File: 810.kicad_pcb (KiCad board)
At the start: 2 copper layers, 148 x 110 mm, 334 parts, among them J1 PJ301BM, J10 PJ301BM, J11 PJ301BM, J12 PJ301BM, J13 PJ301BM, J14 PJ301BM, J15 JACK_MONO_SW, J16 PJ301BM, J17 PJ301B, J18 PJ301B, J2 PJ301BM, J3 PJ301BM, J4 PJ301B, J5 PJ301B, J6 PJ301BM, J7 PJ301BM, J8 PJ301BM, J9 PJ301BM, P1 CONN_01X08, P2 CONN_02X05, P3 CONN_01X03, P4 CONN_01X08, P5 CONN_01X02, P6 CONN_02X03, Q1 PMBT2369, Q10 2SK208-GR, Q11 2SC4738, Q12 2SA1832, Q13 2SA1832, Q14 2SA1832, Q15 2SC4738, Q2 2SK208-GR, Q3 2SA1618, Q4 2SC4207, Q5 2SK208-GR, Q6 MMBF4391LT1G, Q7 2SA1832, Q8 PMBT2369, Q9 2SK208-GR, SW1 SPDT, SW2 SPDT, SW3 BF3-1050, SW4 SPDT, SW5 DP6T-ALPHA-SR2511, U1 TL072-, U10 TL072-, U11 TL072-, U12 TA75S558F, U13 TA75S558F, U14 TA75S558F, U15 TA75S558F, U16 TA75S558F, U17 CD4052, U18 TA75S558F, U19 TL072-, U2 TL072-, U20 CD4013, U21 TA75S558F, U3 TL072-, U4 CD40106, U5 CD4027, U6 LM13700, U7 LM13700, U8 LM13700, U9 TL072-

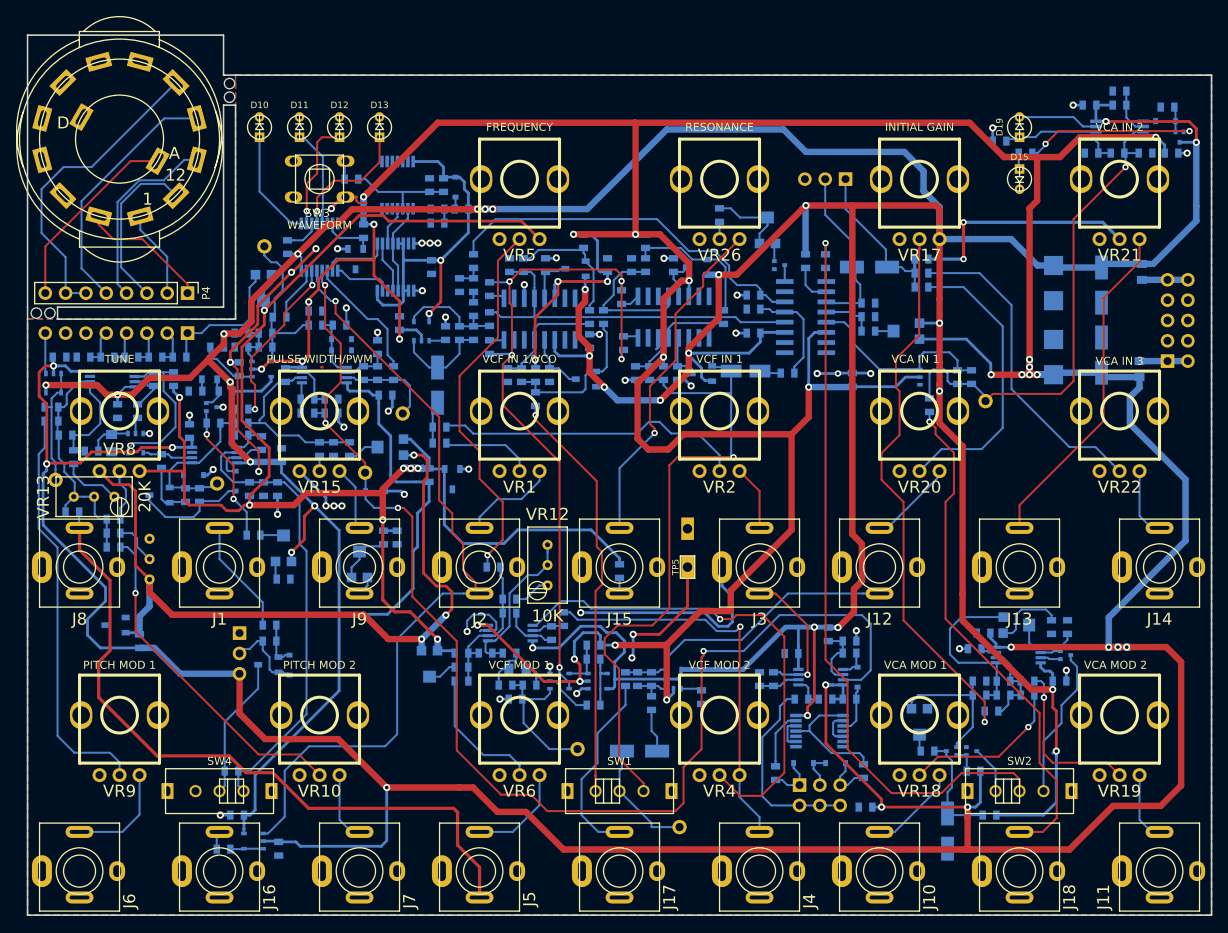
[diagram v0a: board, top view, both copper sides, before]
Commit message: 4 layer version amost done with dedicated ground plane and power plane
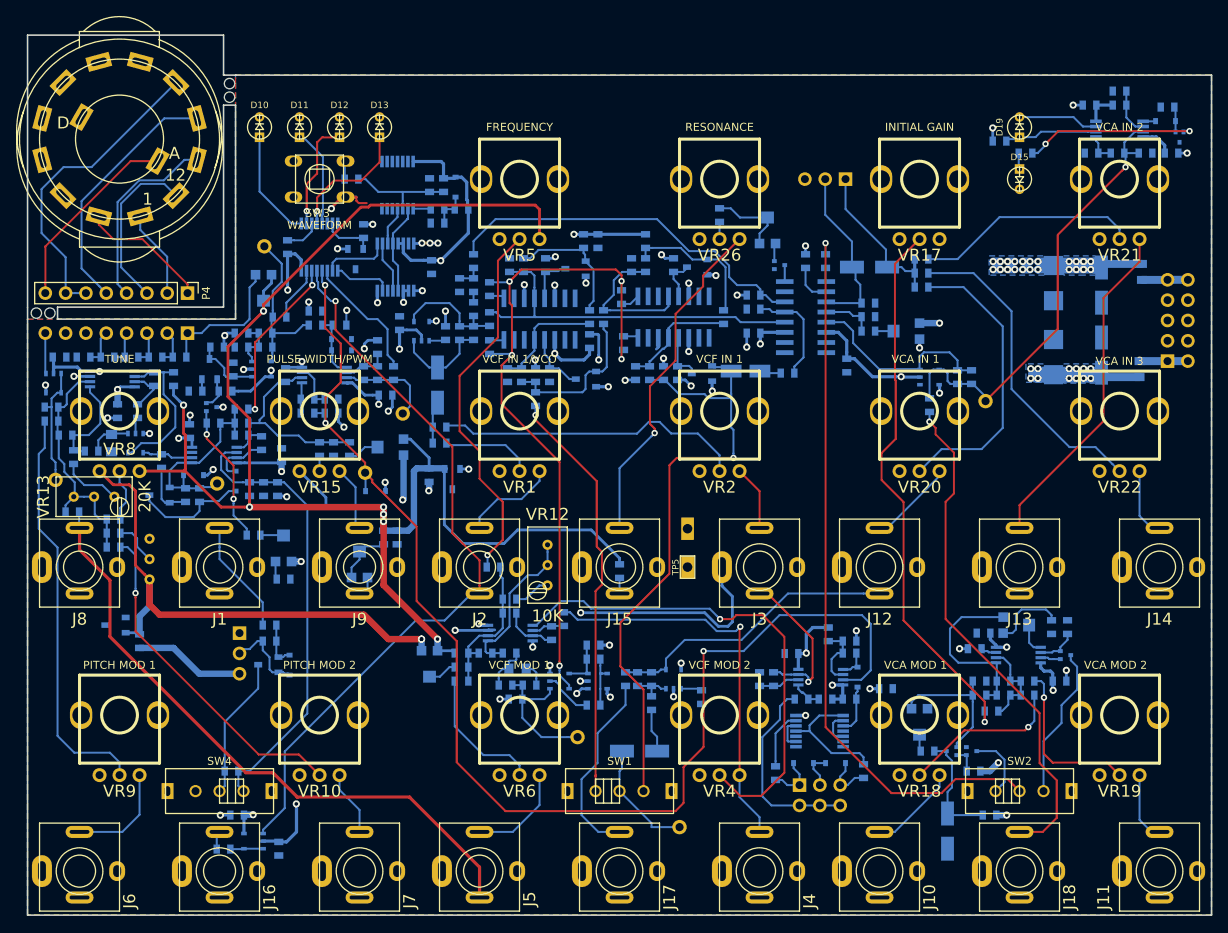
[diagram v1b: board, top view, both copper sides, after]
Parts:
- moved C48 15.0 mm to (191.3, 122.7), turned to 180 degrees
- moved C35 3.23 mm to (155.3, 66.8), turned to 90 degrees
- moved C32 1.93 mm to (186.4, 82.3), turned to 90 degrees
- moved TP1 1.50 mm to (152.8, 128.8)
- moved R68 0.75 mm to (109.7, 82.8)
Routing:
- net -12V: track 825.7 -> 671.8 mm, vias 37 -> 35
- net GND: track 158.1 -> 101.2 mm, vias 50 -> 40
- net +12V: track 734.5 -> 701.3 mm, vias 30 -> 53
- net KYBD: track 88.0 -> 79.1 mm
- net VCO: track 98.9 -> 93.0 mm
- net Net-(C22-Pad2): track 62.8 -> 57.8 mm
- net -10V: track 95.5 -> 91.0 mm
- net Net-(C21-Pad2): track 82.5 -> 78.7 mm
- net +10V: track 198.0 -> 201.4 mm, vias 8 -> 7
- net Net-(Q12-Pad3): track 6.00 -> 8.31 mm
- net SUB_OSC: track 18.2 -> 19.8 mm
- net Net-(R105-Pad2): track 92.4 -> 90.9 mm
- net Net-(R78-Pad1): track 29.4 -> 27.9 mm, vias 2 -> 0
- net VCO_PULSE: track 158.1 -> 159.2 mm, vias 4 -> 3
- net Net-(C3-Pad2): track 13.5 -> 14.4 mm
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- added copper zone on B.Cu, net +12V
- added copper zone on In1.Cu, net +12V
- added copper zone on In1.Cu, net -12V
- added copper zone on In2.Cu, net GND
- removed copper zone on B.Cu, net +10V
- removed copper zone on F.Cu, net +12V
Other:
- copper layers 2 -> 4

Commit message: little more ground plane tweaking required, tidy up silk screen then done
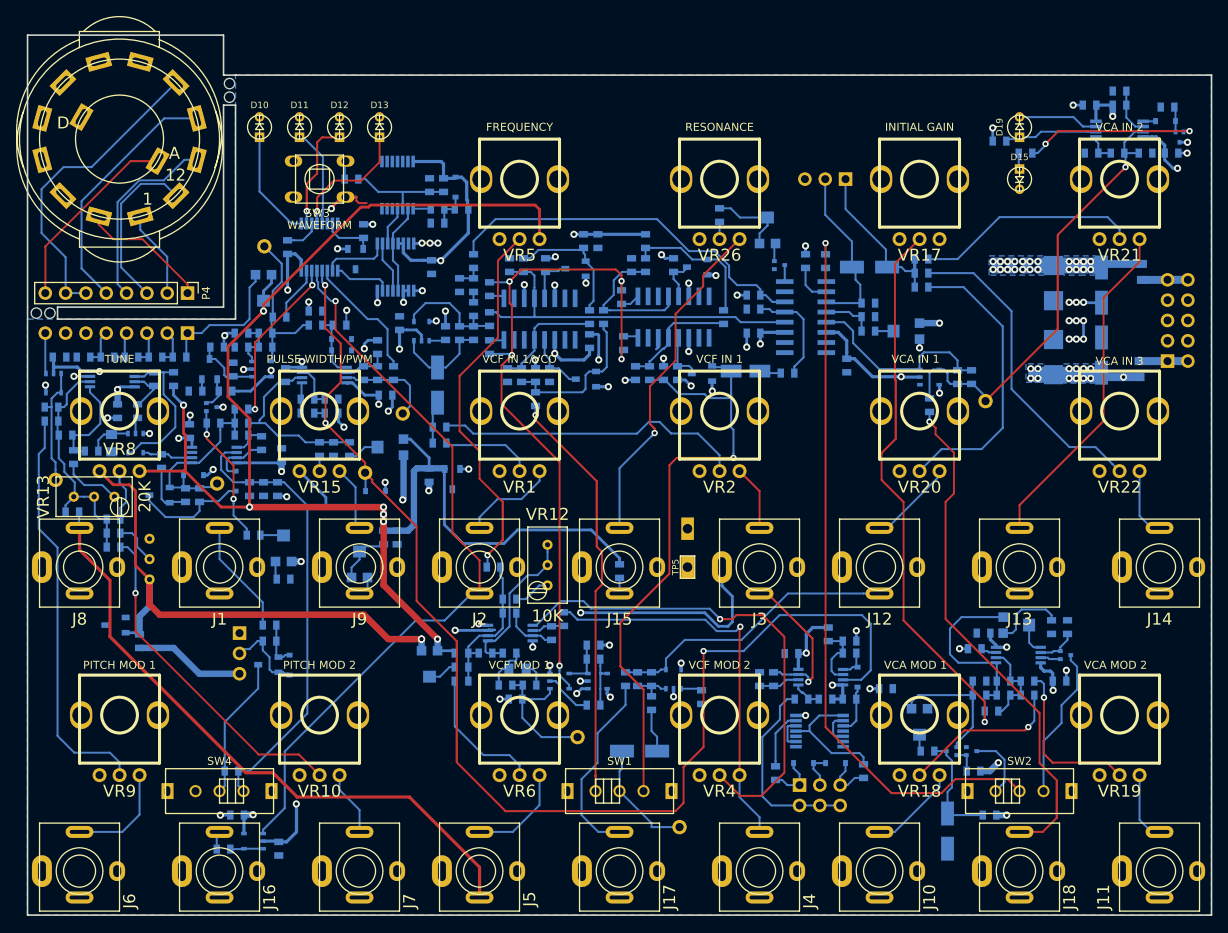
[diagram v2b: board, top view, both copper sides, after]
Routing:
- net +12V: track 701.3 -> 733.2 mm, vias 53 -> 55
- net -12V: track 671.8 -> 703.5 mm, vias 35 -> 37
- net GND: track 101.2 -> 115.8 mm, vias 40 -> 49
- removed copper zone on F.Cu, net GND
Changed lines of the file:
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@@
   (general
     (links 679)
-    (no_connects 4)
-    (area 78.467857 38.411038 232.878334 151.100001)
+    (no_connects 1)
+    (area 83.899999 40.899999 232.100001 151.100001)
     (thickness 1.6)
     (drawings 148)
-    (tracks 2234)
+    (tracks 2275)
     (zones 0)
     (modules 334)
@@
   (layers
     (0 F.Cu signal)
-    (1 In1.Cu power hide)
-    (2 In2.Cu power hide)
+    (1 In1.Cu power)
+    (2 In2.Cu power)
     (31 B.Cu signal)
     (32 B.Adhes user)
@@
   )
   (setup
-    (last_trace_width 0.8)
+    (last_trace_width 0.25)
     (user_trace_width 0.25)
     (user_trace_width 0.4)
@@
   (segment (start 148.635 73.90158) (end 148.635 70.7159) (width 0.25) (layer B.Cu) (net 9))
   (segment (start 148.635 70.7159) (end 148.75 70.6009) (width 0.25) (layer B.Cu) (net 9))
+  (segment (start 215.999998 79) (end 216 78.999998) (width 0.35) (layer In2.Cu) (net 10))
+  (segment (start 215.1 79) (end 215.999998 79) (width 0.35) (layer In2.Cu) (net 10))
+  (segment (start 216 76.7) (end 216 78.999998) (width 0.35) (layer B.Cu) (net 10))
+  (via (at 216 78.999998) (size 0.9) (drill 0.45) (layers F.Cu B.Cu) (net 10))
+  (segment (start 214.2 74.4) (end 214.2 76.7) (width 0.35) (layer In2.Cu) (net 10))
+  (segment (start 214.2 76.7) (end 214.2 79) (width 0.35) (layer In2.Cu) (net 10))
+  (segment (start 215.1 76.7) (end 214.2 76.7) (width 0.35) (layer B.Cu) (net 10))
+  (via (at 214.2 76.7) (size 0.9) (drill 0.45) (layers F.Cu B.Cu) (net 10))
+  (segment (start 216 76.7) (end 215.1 76.7) (width 0.35) (layer In2.Cu) (net 10))
+  (via (at 215.1 76.7) (size 0.9) (drill 0.45) (layers F.Cu B.Cu) (net 10))
+  (via (at 216 76.7) (size 0.9) (drill 0.45) (layers F.Cu B.Cu) (net 10))
+  (segment (start 214.2 79) (end 215.1 79) (width 0.35) (layer B.Cu) (net 10))
+  (via (at 215.1 79) (size 0.9) (drill 0.45) (layers F.Cu B.Cu) (net 10))
+  (via (at 214.2 79) (size 0.9) (drill 0.45) (layers F.Cu B.Cu) (net 10))
+  (segment (start 215.1 74.4) (end 214.2 74.4) (width 0.35) (layer B.Cu) (net 10))
+  (via (at 214.2 74.4) (size 0.9) (drill 0.45) (layers F.Cu B.Cu) (net 10))
+  (segment (start 216 74.4) (end 215.1 74.4) (width 0.35) (layer In2.Cu) (net 10))
+  (via (at 215.1 74.4) (size 0.9) (drill 0.45) (layers F.Cu B.Cu) (net 10))
+  (segment (start 218.25 74.44964) (end 216.04964 74.44964) (width 0.35) (layer B.Cu) (net 10))
+  (segment (start 216.04964 74.44964) (end 216 74.4) (width 0.35) (layer B.Cu) (net 10))
+  (via (at 216 74.4) (size 0.9) (drill 0.45) (layers F.Cu B.Cu) (net 10))
   (segment (start 128.7446 96.9446) (end 128.7 96.9) (width 0.35) (layer B.Cu) (net 10))
   (segment (start 128.7446 98) (end 128.7446 96.9446) (width 0.35) (layer B.Cu) (net 10))
@@
   (segment (start 197.3509 130.5) (end 198.85 130.5) (width 0.25) (layer B.Cu) (net 41))
   (segment (start 199.59874 138.8991) (end 199 138.30036) (width 0.25) (layer B.Cu) (net 41))
+  (segment (start 219.65 60.2) (end 219.65 54.6) (width 0.8) (layer In1.Cu) (net 42))
+  (segment (start 219.85 54.4) (end 219.65 54.6) (width 0.35) (layer In1.Cu) (net 42))
+  (segment (start 219.65 54.6) (end 219.65 51.15) (width 0.8) (layer In1.Cu) (net 42))
+  (segment (start 229 54.4) (end 219.85 54.4) (width 0.35) (layer In1.Cu) (net 42))
+  (segment (start 228 54.4) (end 229 54.4) (width 0.35) (layer B.Cu) (net 42))
+  (via (at 229 54.4) (size 0.9) (drill 0.45) (layers F.Cu B.Cu) (net 42))
+  (segment (start 215.1 69.3) (end 215.1 64.75) (width 0.8) (layer In1.Cu) (net 42))
+  (segment (start 215.1 64.75) (end 219.65 60.2) (width 0.8) (layer In1.Cu) (net 42))
+  (segment (start 219.6491 49.75) (end 219.6491 51.1491) (width 0.8) (layer B.Cu) (net 42))
+  (segment (start 219.6491 51.1491) (end 219.65 51.15) (width 0.8) (layer B.Cu) (net 42))
+  (via (at 219.65 51.15) (size 0.9) (drill 0.45) (layers F.Cu B.Cu) (net 42))
   (segment (start 169.57 85.470002) (end 169.599998 85.5) (width 0.4) (layer B.Cu) (net 42))
   (segment (start 169.57 84.2525) (end 169.57 85.470002) (width 0.4) (layer B.Cu) (net 42))
@@
   (segment (start 212.1 121.7991) (end 212.1491 121.75) (width 0.25) (layer B.Cu) (net 42))
   (segment (start 212.5 70.05036) (end 212.25 69.80036) (width 0.8) (layer B.Cu) (net 42))
-  (segment (start 223 83.75) (end 218.80036 83.75) (width 1) (layer B.Cu) (net 43))
+  (segment (start 223 83.75) (end 221 83.75) (width 1) (layer B.Cu) (net 43))
+  (segment (start 221 83.75) (end 218.80036 83.75) (width 1) (layer B.Cu) (net 43))
+  (segment (start 227.75 65.5) (end 221 72.25) (width 0.8) (layer In1.Cu) (net 43))
+  (segment (start 221 72.25) (end 221 83.75) (width 0.8) (layer In1.Cu) (net 43))
+  (via (at 221 83.75) (size 0.9) (drill 0.45) (layers F.Cu B.Cu) (net 43))
+  (segment (start 227.75 57.65) (end 227.75 65.5) (width 0.8) (layer In1.Cu) (net 43))
+  (segment (start 226.1491 55.75) (end 226.1491 56.5991) (width 0.35) (layer B.Cu) (net 43))
+  (segment (start 226.1491 56.5991) (end 227.2 57.65) (width 0.35) (layer B.Cu) (net 43))
+  (segment (start 227.2 57.65) (end 227.75 57.65) (width 0.35) (layer B.Cu) (net 43))
+  (via (at 227.75 57.65) (size 0.9) (drill 0.45) (layers F.Cu B.Cu) (net 43))
   (segment (start 218.80036 83.75) (end 218.25 83.19964) (width 1) (layer B.Cu) (net 43))
   (segment (start 205.35 131.95) (end 205.35 130.4) (width 0.8) (layer In1.Cu) (net 43))
@@
       )
     )
-  )
-  (zone (net 10) (net_name GND) (layer F.Cu) (hatch edge 0.508)
-    (connect_pads (clearance 0.254))
-    (min_thickness 0.2032)
-    (fill yes (arc_segments 16) (thermal_gap 0.254) (thermal_bridge_width 0.5048))
-    (polygon
-      (pts
-        (xy 110 46) (xy 232 46) (xy 232 151) (xy 84 151) (xy 84 76.5)
-        (xy 110 76.5) (xy 110 47)
-      )
-    )

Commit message: moved rotary switch to its own PCB
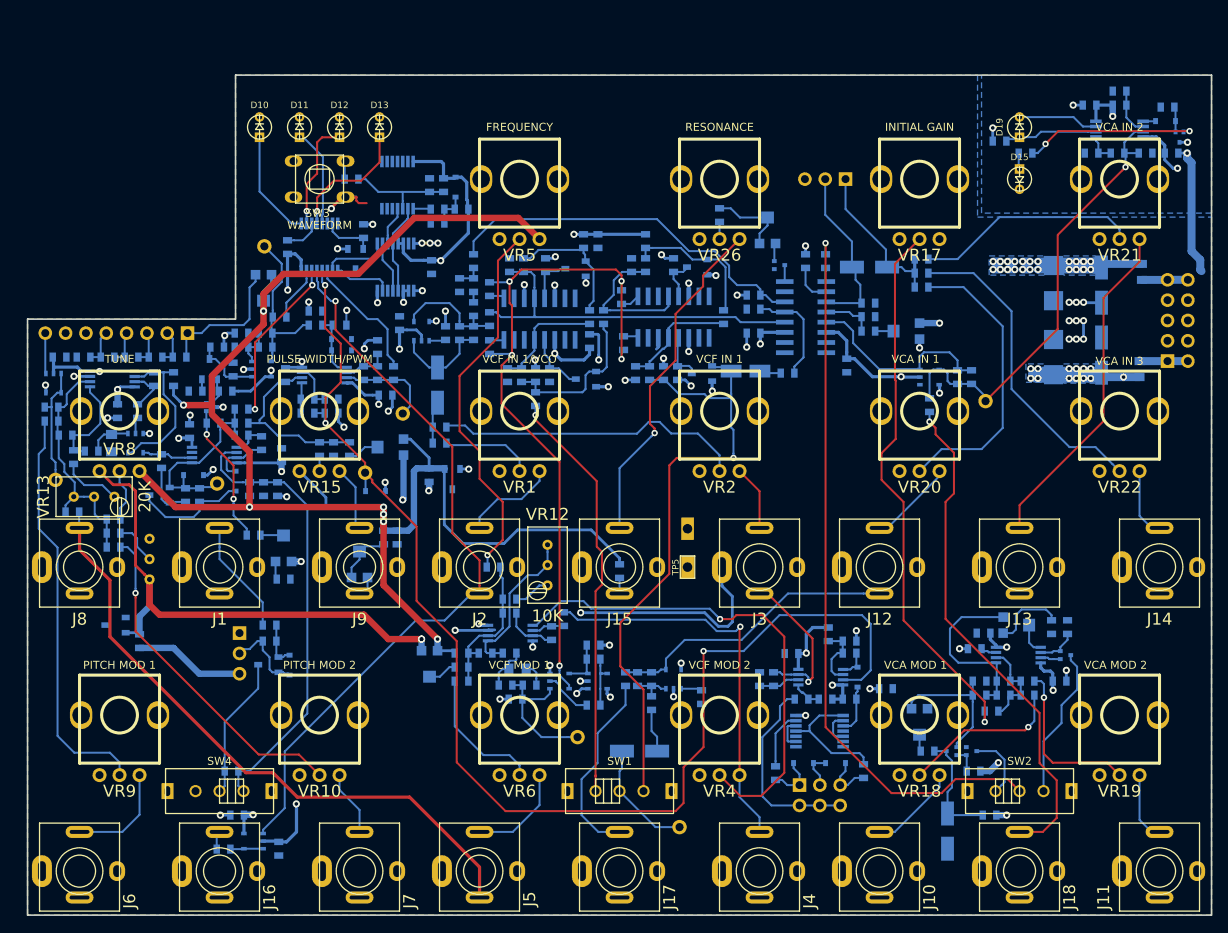
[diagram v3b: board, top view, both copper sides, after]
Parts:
- removed P4: CONN_01X08, Pin_Headers:Pin_Header_Straight_1x08_Pitch2.54mm
- removed SW5: DP6T-ALPHA-SR2511, MyModules:SR2511-ALPHA
- removed the TP7 at (109.2, 47.1)
- removed the TP7 at (109.2, 48.8)
- removed the TP7 at (85.1, 75.8)
- removed the TP7 at (86.8, 75.8)
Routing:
- net Net-(P4-Pad6): track 39.1 -> 0.00 mm
- net Net-(P4-Pad5): track 31.5 -> 0.00 mm
- net Net-(P4-Pad8): track 24.3 -> 0.00 mm
- net Net-(P4-Pad4): track 23.9 -> 0.00 mm
- net Net-(P4-Pad3): track 21.0 -> 0.00 mm
- net Net-(P4-Pad1): track 16.3 -> 0.00 mm
- net GND: track 115.8 -> 131.3 mm
- net Net-(P4-Pad2): track 11.0 -> 0.00 mm
- net +10V: track 201.4 -> 195.5 mm
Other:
- board size 148 x 110 mm -> 148 x 105 mm

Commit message: bit of tweaking. ready to order
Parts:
- TC1: footprint MyModules:SM0805-HAND -> MyModules:SM0603-R-JRL
- moved R128 4.78 mm to (220.2, 59.0), turned to 0 degrees
- moved TC1 0.22 mm to (94.7, 91.9)
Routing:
- net GND: track 131.3 -> 123.7 mm, vias 49 -> 54
- net Net-(C21-Pad2): track 78.7 -> 76.3 mm
- net KYBD: track 79.1 -> 81.1 mm
- net Net-(J18-Pad3): track 64.0 -> 63.3 mm
- net Net-(R78-Pad1): track 27.9 -> 27.3 mm

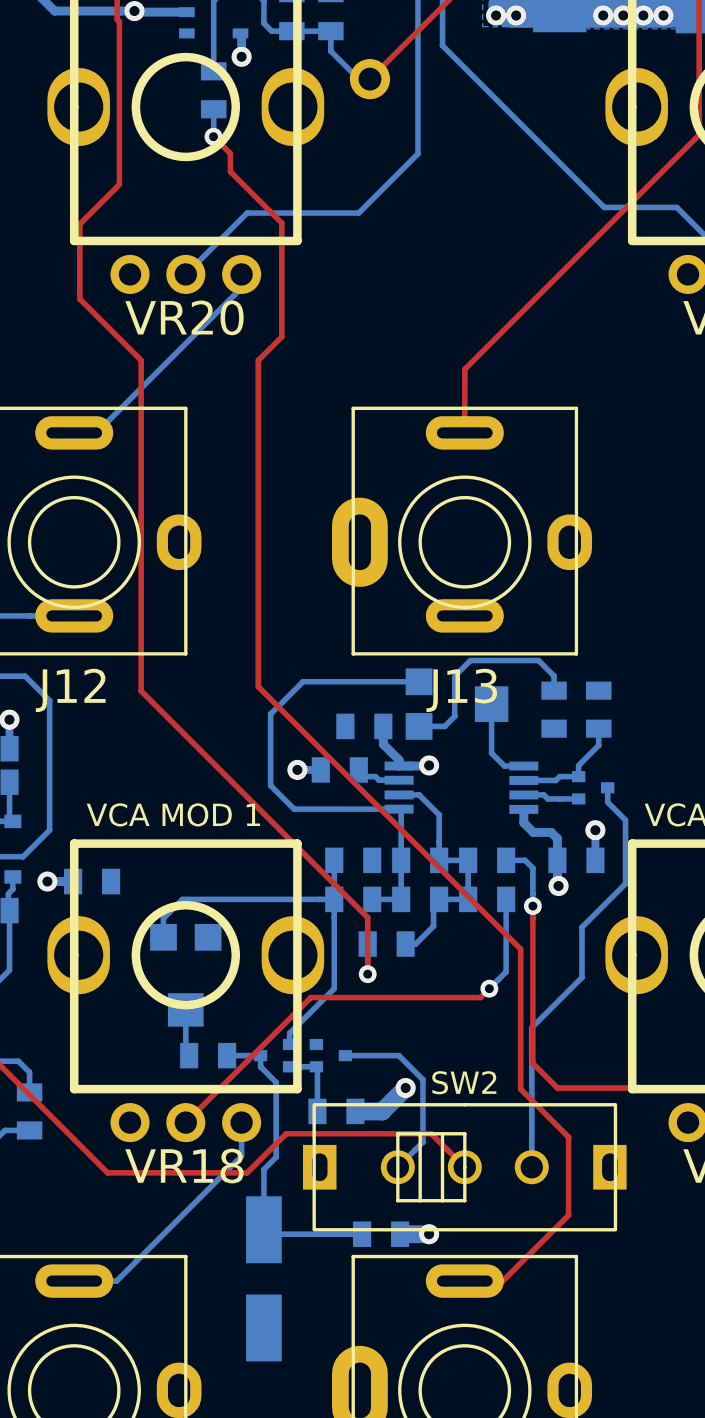
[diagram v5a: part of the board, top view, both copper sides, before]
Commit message: changed a couple of schematic notes
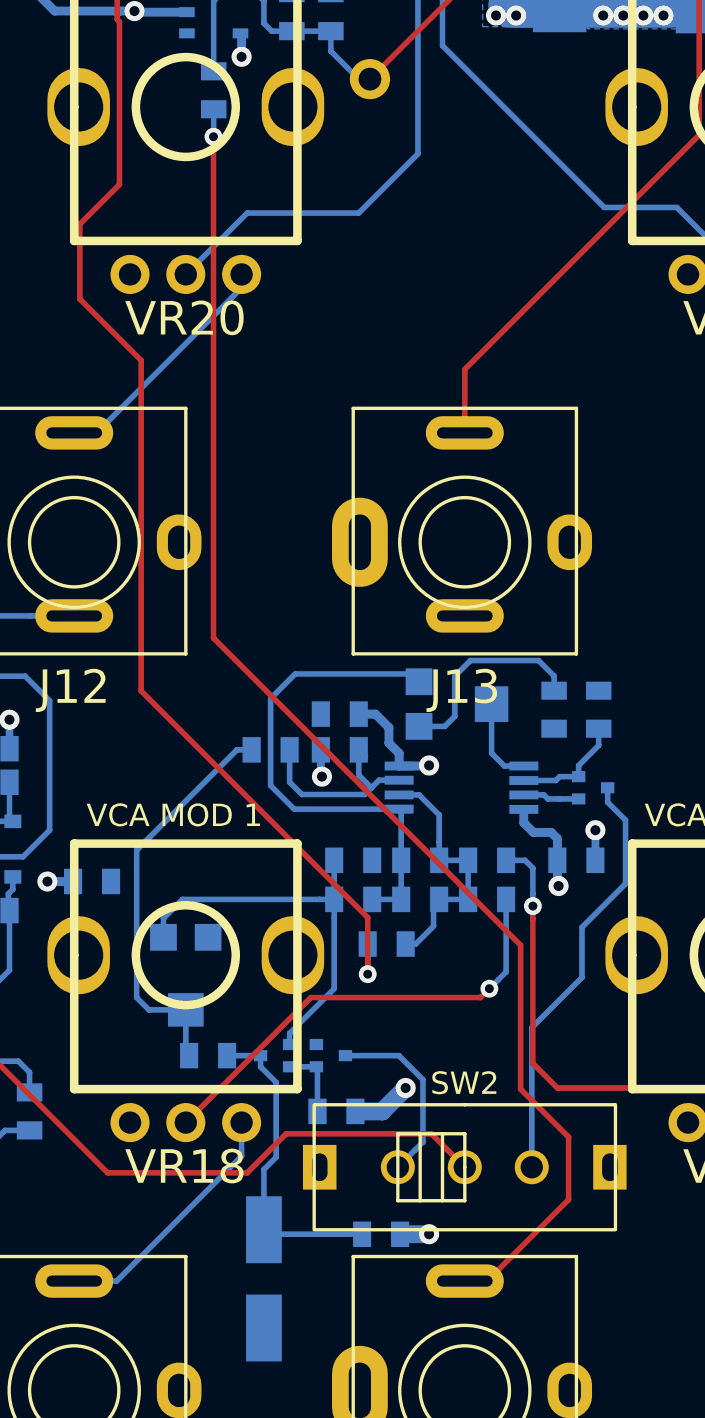
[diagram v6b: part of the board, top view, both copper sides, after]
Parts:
- added R86: 270K, MyModules:SM0603-R-JRL, B.Cu at (199.3, 116.8)
- C45, C46: value 10μF -> 47μF
- R137: value 15K -> 330
- R3: value 2.2K -> 220
- R55: value 22K -> 1K
- R59: value 1meg -> 470K
- R91: value 15K -> 10K
- moved C28 1.23 mm to (202.4, 115.2)
- moved R137 0.90 mm to (202.4, 116.8)
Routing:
- net Net-(R86-Pad2): track 2.11 -> 18.2 mm
- net Net-(R137-Pad2): track 2.00 -> 9.21 mm
- net -12V: track 703.7 -> 705.2 mm
- net Net-(J18-Pad3): track 63.3 -> 62.0 mm
- net Net-(C16-Pad2): track 22.0 -> 22.7 mm
